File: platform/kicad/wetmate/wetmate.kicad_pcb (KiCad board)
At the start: 2 copper layers, 20.6 x 15.5 mm, 2 parts, among them J1 Screw_Terminal_01x03, J2 Screw_Terminal_01x03

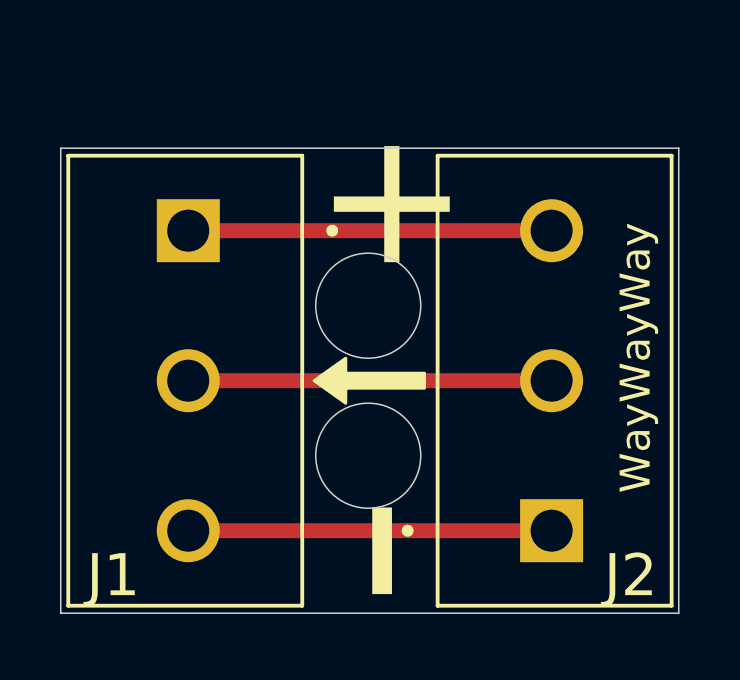
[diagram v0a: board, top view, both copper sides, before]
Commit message: Wetmate: Wetmate v1revB
This change further increases the width of the traces and updates the ID
number to match the JLC standard.
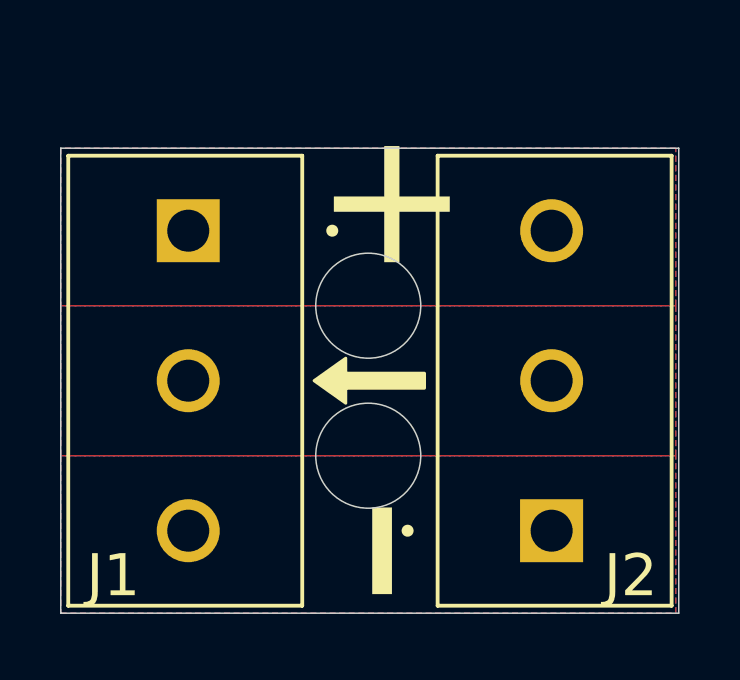
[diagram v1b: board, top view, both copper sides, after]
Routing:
- net /Vss: track 12.1 -> 0.00 mm
- net /Vdd: track 12.1 -> 0.00 mm
- net /Signal: track 12.1 -> 0.00 mm
- added copper zone on B.Cu, net /Signal
- added copper zone on F.Cu, net /Signal
- added copper zone on B.Cu, net /Vdd
- added copper zone on F.Cu, net /Vdd
- added copper zone on B.Cu, net /Vss
- added copper zone on F.Cu, net /Vss
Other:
- board text removed: "WayWayWay"
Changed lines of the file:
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@@
 			(drillshape 0)
 			(scaleselection 1)
-			(outputdirectory "gerber/")
+			(outputdirectory "production/v1revB/")
 		)
 	)
@@
 		(at 109 67.5 -90)
 		(property "Reference" "J1"
-			(at 11.5 2.5 360)
+			(at 11.5 2.5 0)
 			(layer "F.SilkS")
 			(effects
@@
 	)
 	(gr_rect
+		(start 110.75 67.5)
+		(end 112.75 77.5)
+		(stroke
+			(width 0.1)
+			(type solid)
+		)
+		(fill solid)
+		(layer "B.SilkS")
+	)
+	(gr_rect
 		(start 113.875 72.25)
 		(end 116.875 72.75)
@@
 		)
 	)
-	(gr_text "WayWayWay"
-		(at 124.5 76.25 90)
-		(layer "F.SilkS")
-		(effects
-			(font
-				(size 1 1)
-				(thickness 0.1)
-			)
-			(justify left bottom)
-		)
-	)
 	(gr_text "+"
 		(at 113.2 69.1 0)
@@
 		)
 	)
-	(segment
-		(start 109 72.5)
-		(end 121.1125 72.5)
-		(width 0.5)
-		(layer "F.Cu")
+	(zone
+		(net 2)
+		(net_name "/Vdd")
+		(layers "F&B.Cu")
+		(hatch edge 0.5)
+		(priority 1)
+		(connect_pads
+			(clearance 0.5)
+		)
+		(min_thickness 0.25)
+		(filled_areas_thickness no)
+		(fill yes
+			(thermal_gap 0.5)
+			(thermal_bridge_width 0.5)
+		)
+		(polygon
+			(pts
+				(xy 104.75 70) (xy 125.25 70) (xy 125.25 64.75) (xy 104.75 64.75)
+			)
+		)
+	)
+	(zone
 		(net 1)
-	)
-	(segment
-		(start 109 67.5)
-		(end 121.1125 67.5)
-		(width 0.5)
-		(layer "F.Cu")
-		(net 2)
-	)
-	(segment
-		(start 109 77.5)
-		(end 121.1125 77.5)
-		(width 0.5)
-		(layer "F.Cu")
+		(net_name "/Signal")
+		(layers "F&B.Cu")
+		(hatch edge 0.5)
+		(connect_pads
+			(clearance 0.5)
+		)
+		(min_thickness 0.25)
+		(filled_areas_thickness no)
+		(fill yes
+			(thermal_gap 0.5)
+			(thermal_bridge_width 0.5)
+		)
+		(polygon
+			(pts
+				(xy 104.75 75) (xy 125.25 75) (xy 125.25 70) (xy 104.75 70)
+			)
+		)
+	)
+	(zone
 		(net 3)
+		(net_name "/Vss")
+		(layers "F&B.Cu")
+		(hatch edge 0.5)
+		(priority 1)
+		(connect_pads
+			(clearance 0.5)
+		)
+		(min_thickness 0.25)
+		(filled_areas_thickness no)
+		(fill yes
+			(thermal_gap 0.5)
+			(thermal_bridge_width 0.5)
+		)
+		(polygon
+			(pts
+				(xy 104.75 80.25) (xy 125.25 80.25) (xy 125.25 75) (xy 104.75 75)
+			)
+		)
 	)
 )
